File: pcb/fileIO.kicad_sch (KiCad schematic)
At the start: 32 parts, among them J1 Conn_01x12_Male, J2 Conn_01x16_Male, J3 USB_B_Micro, SW1 SW_Push, U9 74HC4067BQ

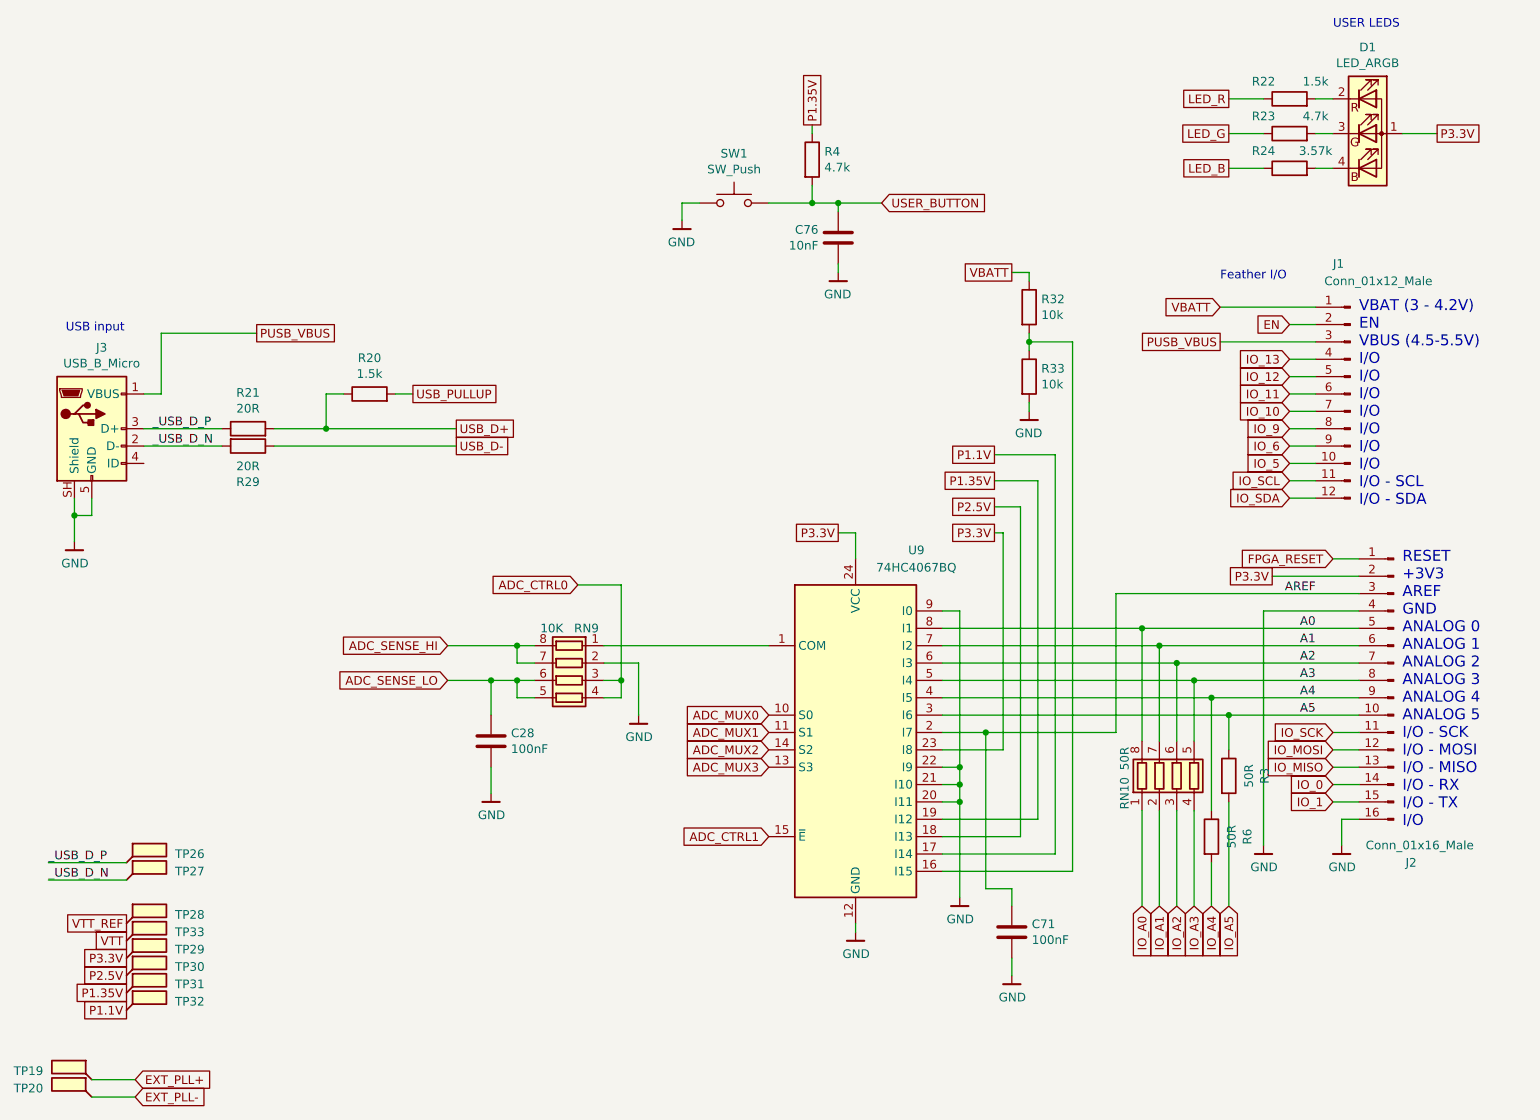
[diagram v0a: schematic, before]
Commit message: refactor(pcb): strip down
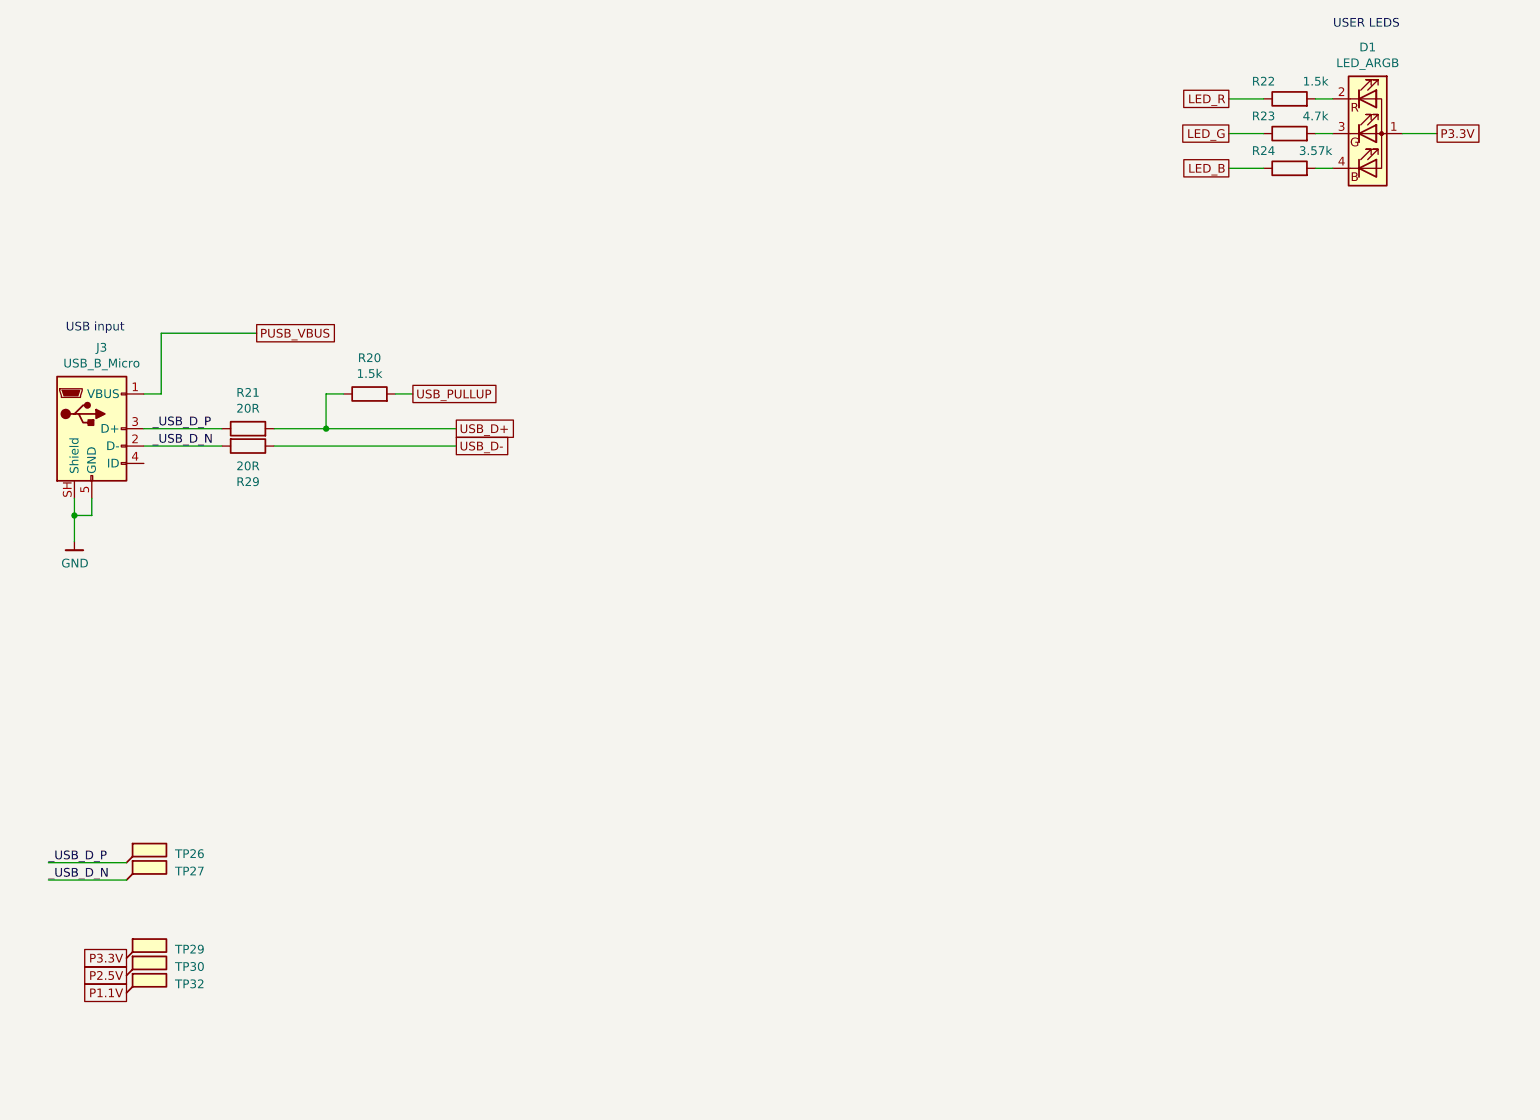
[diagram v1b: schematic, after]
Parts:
- removed C28, C71: 100nF, Capacitor_SMD:C_0201_0603Metric, symbol Device:C
- removed C76: 10nF, Capacitor_SMD:C_0201_0603Metric, symbol Device:C
- removed J1: Conn_01x12_Male, gkl_conn:Feather_PinHeader_1x12, symbol Connector:Conn_01x12_Male
- removed J2: Conn_01x16_Male, gkl_conn:Feather_PinHeader_1x16, symbol Connector:Conn_01x16_Male
- removed R3, R6: 50R, Resistor_SMD:R_0201_0603Metric, symbol Device:R
- removed R32, R33: 10k, Resistor_SMD:R_0201_0603Metric, symbol Device:R
- removed R4: 4.7k, Resistor_SMD:R_0201_0603Metric, symbol Device:R
- removed RN10: 50R, Resistor_SMD:R_Array_Convex_4x0402, symbol Device:R_Pack04
- removed RN9: 10K, Resistor_SMD:R_Array_Convex_4x0402, symbol Device:R_Pack04
- removed SW1: SW_Push, gkl_misc:PTS_810_SMT_Switch, symbol Switch:SW_Push
- removed TP19, TP20, TP28, TP31, TP33: SMD_TP, gkl_misc:TestPoint_Pad_D0.5mm, symbol Connector:TestPoint_Flag
- removed U9: 74HC4067BQ, Package_DFN_QFN:Texas_RGY_R-PVQFN-N24_EP2.05x3.1mm, symbol 74xx:CD74HC4067M
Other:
- note removed: "Feather I/O"
- note removed: "RESET +3V3 AREF GND ANALOG 0 ANALOG 1 ANALOG 2 ANALOG 3 ANALOG 4 ANALOG 5 I/O - SCK I/O - MOSI I/O - MISO I/O - RX I/O - TX I/O"
- note removed: "VBAT (3 - 4.2V) EN VBUS (4.5-5.5V) I/O I/O I/O I/O I/O I/O I/O I/O - SCL I/O - SDA"
- moved on the sheet: TP32
